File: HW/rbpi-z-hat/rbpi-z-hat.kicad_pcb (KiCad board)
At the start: 4 copper layers, 65 x 30 mm, 96 parts, among them IC1 BQ24315DSGR, J1 RBPI_CONN, J10 JST_GH, J2 Conn_01x10, J3 Conn_01x10, J4 Conn_01x10, J5 Conn_01x06, J6 Conn_01x06, J7 Conn_01x06, J8 Conn_01x06_MountingPin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

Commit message: Some changes in Sch & PCB
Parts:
- L5, L6, L7, L8: moved to B.Cu
- moved C1 81.6 mm to (24.8, 46.8)
- moved L8 46.3 mm to (36.8, 7.75)
- moved L7 46.2 mm to (35.0, 7.75)
- moved C23 42.8 mm to (25.0, 18.0), turned to 180 degrees
- moved L6 42.5 mm to (33.2, 7.75)
- moved L5 42.4 mm to (31.5, 7.75)
- moved C25 41.5 mm to (25.1, 16.0), turned to 180 degrees
- moved C26 40.6 mm to (25.1, 14.4), turned to 180 degrees
- moved C30 40.1 mm to (32.8, 15.0), turned to 270 degrees
- moved C27 39.9 mm to (28.1, 19.3), turned to 270 degrees
- moved C24 37.9 mm to (29.7, 19.3), turned to 270 degrees
- moved U8 35.5 mm to (29.2, 15.0), turned to 90 degrees
- moved U9 35.2 mm to (35.8, 15.0), turned to 180 degrees
- moved C28 35.2 mm to (34.8, 11.4), turned to 90 degrees
- moved C29 32.6 mm to (36.8, 11.6), turned to 90 degrees
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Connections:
- J1 pad 19: /rbpi/SPI0_MOSI -> /SPI0_MOSI
- J1 pad 21: /rbpi/SPI0_MISO -> /SPI0_MISO
- J1 pad 23: /rbpi/SPI0_SCLK -> /SPI0_SCK
- L5 pad 1: (no net) -> /SENS_MOSI
- L5 pad 2: (no net) -> /SPI0_MOSI
- L6 pad 1: (no net) -> /SENS_MISO
- L6 pad 2: (no net) -> /SPI0_MISO
- L7 pad 1: (no net) -> /SENS_SCK
- L7 pad 2: (no net) -> /SPI0_SCK
- RN7 pad 1: /rbpi/SPI0_MOSI -> /SPI0_MOSI
- RN7 pad 2: /rbpi/SPI0_MISO -> /SPI0_MISO
- RN7 pad 3: /rbpi/SPI0_SCLK -> /SPI0_SCK
- U6 pad 10: (no net) -> /SCL1
- U6 pad 9: (no net) -> /SDA1
- U8 pad 2: /IMU/IMU_SCK -> /SENS_SCK
- U8 pad 4: /IMU/IMU_MOSI -> /SENS_MOSI
- U8 pad 5: /IMU/IMU_MISO -> /SENS_MISO
- U8 pad 6: /IMU/IMU_MISO -> /SENS_MISO
- U9 pad 1: /IMU/IMU_MISO -> /SENS_MISO
- U9 pad 13: /IMU/IMU_SCK -> /SENS_SCK
- U9 pad 14: /IMU/IMU_MOSI -> /SENS_MOSI

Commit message: Changes in Sch
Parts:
- removed C20, C21: 22uF/10V, Capacitor_SMD:C_1206_3216Metric
- removed U7: MIC5504-3.3YM5, Package_TO_SOT_SMD:SOT-23-5
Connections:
- net /SENSORS_POWER/sheet5EE7A825/MIC_VIN renamed /SENSORS_POWER/MIC5504/MIC_VIN
- C12 pad 1: /SENSORS_POWER/SENS_VIN -> /BQ24313_OUT
- C12 pad 2: /SENSORS_POWER/SENS_GND -> GNDD
- IC1 pad 8: /BQ24313/BQ_OUT -> /BQ24313_OUT
- L2 pad 1: /SENSORS_POWER/SENS_VIN -> /BQ24313_OUT
- L3 pad 1: /SENSORS_POWER/SENS_GND -> GNDD

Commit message: Changes in Schematics
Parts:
- added R11: 10K, Resistor_SMD:R_0603_1608Metric, F.Cu at (21.6, -12.3)
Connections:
- net /PCA9685/PCA_nOE renamed /PCA_nOE
- net /rbpi/SPI1_CE2 renamed /rbpi/SPI0_CE0
- J1 pad 26: (no net) -> /rbpi/SPI0_CE1
- J1 pad 7: /rbpi/Pin_7_PPM_SBUS_INPUT -> /rbpi/GPIO_4
- R6 pad 1: (no net) -> /rbpi/GPIO_4
- RN6 pad 3: /rbpi/Pin_7_PPM_SBUS_INPUT -> /rbpi/GPIO_4
- U2 pad 6: /BARO/BARO_MISO -> /SENS_MISO
- U2 pad 7: /BARO/BARO_MOSI -> /SENS_MOSI
- U2 pad 8: /BARO/BARO_SCK -> /SENS_SCK
- U5 pad 3: /BARO/BARO_MOSI -> /SENS_MOSI
- U5 pad 4: /BARO/BARO_SCK -> /SENS_SCK
- U5 pad 5: /BARO/BARO_MISO -> /SENS_MISO

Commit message: Update
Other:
- net class 6mils removed
- net class Default removed

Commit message: Some new things...
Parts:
- added U7: STM32F031G6Ux, Package_DFN_QFN:QFN-28-1EP_4x4mm_P0.4mm_EP2.6x2.6mm_ThermalVias, F.Cu at (41.3, 16.6)
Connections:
- net /rbpi/GPIO_4 renamed /rbpi/Pin_7_PPM_SBUS_INPUT
- net Net-(J3-Pad1) renamed /PCA9685/SERVO_POWER
- IC1 pad 3: (no net) -> unconnected-(IC1-NC-Pad3)
- IC1 pad 4: (no net) -> /BQ24313/BQ_nFAULT
- J1 pad 11: (no net) -> /rbpi/Pin_11_UART_RTS
- J1 pad 12: (no net) -> /rbpi/Pin_12_UART_CTS
- J1 pad 13: (no net) -> /rbpi/Pin_13_PWM_EN
- J1 pad 15: (no net) -> /rbpi/GPIO_22
- J1 pad 16: (no net) -> /rbpi/Pin_16_MPU_DRDY
- J1 pad 18: (no net) -> /rbpi/Pin_18
- J1 pad 22: (no net) -> /rbpi/Pin_22
- J1 pad 24: /rbpi/SPI0_CE0 -> /LSM_nCS
- J1 pad 26: /rbpi/SPI0_CE1 -> /BMP_nCS
- J1 pad 27: (no net) -> /rbpi/GPIO_0_HAT_SDA
- J1 pad 28: (no net) -> /rbpi/GPIO_1_HAT_SCL
- J1 pad 29: (no net) -> /rbpi/GPIO_5
- J1 pad 31: (no net) -> /rbpi/GPIO_6
- J1 pad 32: (no net) -> /rbpi/GPIO_12
- J1 pad 33: (no net) -> /rbpi/GPIO_13
- J1 pad 35: (no net) -> /rbpi/GPIO_19
- J1 pad 36: (no net) -> /rbpi/Pin_36
- J1 pad 37: (no net) -> /rbpi/GPIO_26
- J1 pad 38: (no net) -> /rbpi/Pin_38
- J1 pad 40: (no net) -> /rbpi/Pin_40
- L8 pad 1: (no net) -> /FB/Y4
- L8 pad 2: (no net) -> /FB/X4
- R11 pad 2: /rbpi/SPI0_CE1 -> /BMP_nCS
- RN6 pad 4: (no net) -> unconnected-(RN6-R4.1-Pad4)
- RN6 pad 6: (no net) -> /rbpi/SBUS_INPUT_RAW
- RN7 pad 4: /rbpi/SPI0_CE0 -> /LSM_nCS
- U1 pad 3: (no net) -> /SENSORS_EN
- U1 pad 4: (no net) -> unconnected-(U1-NC-Pad4)
- U5 pad 2: (no net) -> /BMP_nCS
- U6 pad 2: (no net) -> unconnected-(U6-ALERT/RDY-Pad2)
- U6 pad 6: (no net) -> /ADS1015/AIN2
- U6 pad 7: (no net) -> /ADS1015/AIN3
- U8 pad 10: (no net) -> /IMU/LSM_INT3
- U8 pad 11: (no net) -> /IMU/LSM_INT1
- U8 pad 12: (no net) -> /IMU/LSM_INT2
- U8 pad 13: (no net) -> /IMU/LSM_DEN
- U8 pad 7: /IMU/LSM_nCS -> /LSM_nCS
- U8 pad 8: /IMU/LSM_nCS -> /LSM_nCS
- U8 pad 9: (no net) -> /IMU/LSM_INT4
- U9 pad 10: Net-(U9-Pad10) -> unconnected-(U9-RESV-Pad10)
- U9 pad 11: Net-(U9-Pad10) -> unconnected-(U9-RESV-Pad11)
- U9 pad 12: (no net) -> /IMU/ICM_nCS
- U9 pad 2: Net-(U9-Pad10) -> unconnected-(U9-RESV-Pad2)
- U9 pad 3: Net-(U9-Pad10) -> unconnected-(U9-RESV-Pad3)
- U9 pad 4: (no net) -> /IMU/ICM_INT1
- U9 pad 7: Net-(U9-Pad10) -> unconnected-(U9-RESV-Pad7)
- U9 pad 9: (no net) -> /IMU/ICM_INT2
- X1 pad 1: (no net) -> unconnected-(X1-EN-Pad1)

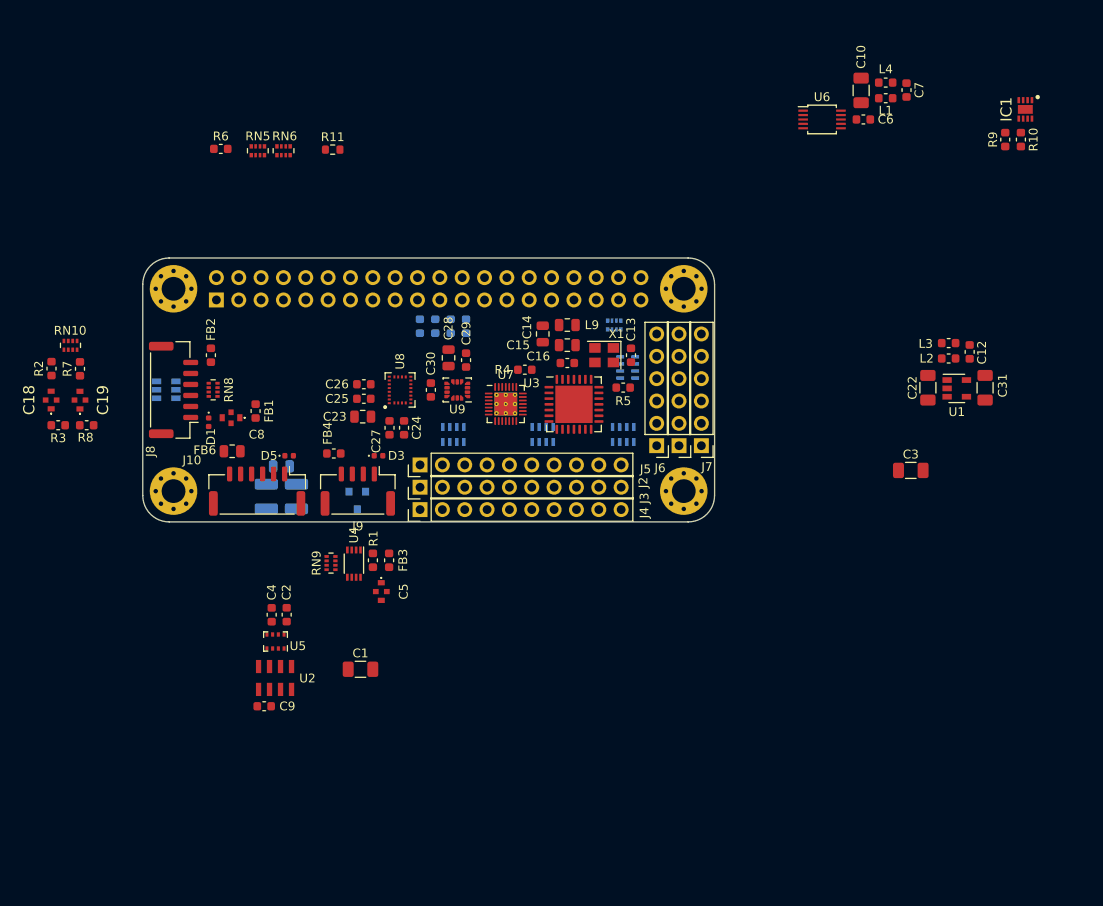
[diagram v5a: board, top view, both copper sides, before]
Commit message: PCA and ADC replaced by CH32V203G6U6
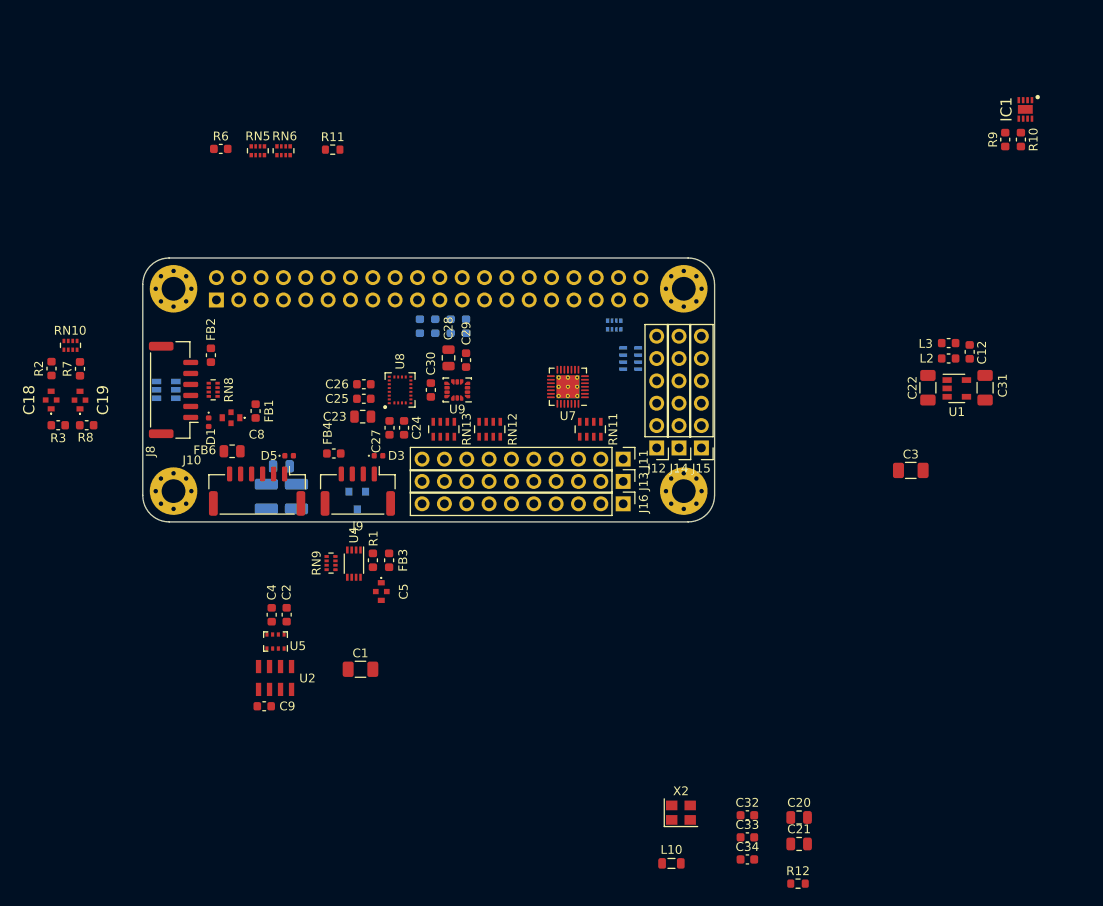
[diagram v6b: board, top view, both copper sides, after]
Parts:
- removed C10: 22uF/10V, Capacitor_SMD:C_1206_3216Metric
- removed C13, C16, C6: 0.1uF, Capacitor_SMD:C_0603_1608Metric
- removed C14, C15: 10uF, Capacitor_SMD:C_0805_2012Metric
- removed C7: 100nF, Capacitor_SMD:C_0603_1608Metric
- removed J2, J3, J4: Conn_01x10, Connector_PinHeader_2.54mm:PinHeader_1x10_P2.54mm_Vertical
- removed J5, J6, J7: Conn_01x06, Connector_PinHeader_2.54mm:PinHeader_1x06_P2.54mm_Vertical
- removed L1, L4: Ferrite_Bead, Inductor_SMD:L_0603_1608Metric
- removed L9: Ferrite_Bead, Inductor_SMD:L_0805_2012Metric
- removed R4, R5: 10K, Resistor_SMD:R_0603_1608Metric
- removed RN1, RN2, RN3, RN4: 220R, Resistor_SMD:R_Array_Concave_4x0603
- removed U3: PCA9685BS, Package_DFN_QFN:QFN-28-1EP_6x6mm_P0.65mm_EP4.25x4.25mm
- removed U6: ADS1015IDGS, Package_SO:TSSOP-10_3x3mm_P0.5mm
- removed X1: ASEMB-25.000MHZ-LC-T, Oscillator:Oscillator_SMD_Abracon_ASE-4Pin_3.2x2.5mm
- added C20: 10uF, Capacitor_SMD:C_0805_2012Metric, F.Cu at (74.6, 63.6)
- added C21: 10uF, Capacitor_SMD:C_0805_2012Metric, F.Cu at (74.6, 66.6)
- added C32: 0.1uF, Capacitor_SMD:C_0603_1608Metric, F.Cu at (68.7, 63.4)
- added C33: 0.1uF, Capacitor_SMD:C_0603_1608Metric, F.Cu at (68.7, 65.9)
- added C34: 0.1uF, Capacitor_SMD:C_0603_1608Metric, F.Cu at (68.7, 68.4)
- added J11: Conn_01x10, Connector_PinHeader_2.54mm:PinHeader_1x10_P2.54mm_Vertical, F.Cu at (54.6, 22.9)
- added J12: Conn_01x06, Connector_PinHeader_2.54mm:PinHeader_1x06_P2.54mm_Vertical, F.Cu at (58.4, 21.6)
- added J13: Conn_01x10, Connector_PinHeader_2.54mm:PinHeader_1x10_P2.54mm_Vertical, F.Cu at (54.6, 25.4)
- added J14: Conn_01x06, Connector_PinHeader_2.54mm:PinHeader_1x06_P2.54mm_Vertical, F.Cu at (61.0, 21.6)
- added J15: Conn_01x06, Connector_PinHeader_2.54mm:PinHeader_1x06_P2.54mm_Vertical, F.Cu at (63.5, 21.6)
- added J16: Conn_01x10, Connector_PinHeader_2.54mm:PinHeader_1x10_P2.54mm_Vertical, F.Cu at (54.6, 27.9)
- added L10: Ferrite_Bead, Inductor_SMD:L_0805_2012Metric, F.Cu at (60.1, 68.8)
- added R12: 10K, Resistor_SMD:R_0603_1608Metric, F.Cu at (74.5, 71.1)
- added RN11: 220R, Resistor_SMD:R_Array_Concave_4x0603, F.Cu at (50.9, 19.5)
- added RN12: 220R, Resistor_SMD:R_Array_Concave_4x0603, F.Cu at (39.4, 19.5)
- added RN13: 220R, Resistor_SMD:R_Array_Concave_4x0603, F.Cu at (34.2, 19.5)
- added RN14: 220R, Resistor_SMD:R_Array_Concave_4x0603, B.Cu at (55.5, 11.4)
- added X2: ASEMB-25.000MHZ-LC-T, Oscillator:Oscillator_SMD_Abracon_ASE-4Pin_3.2x2.5mm, F.Cu at (61.2, 63.1)
- moved U7 7.33 mm to (48.3, 14.6), turned to 180 degrees
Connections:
- U7 pad 10: unconnected-(U7-PA4-Pad10) -> /SDA1
- U7 pad 11: unconnected-(U7-PA5-Pad11) -> /CH32V203G6U6/PWM_OUT7
- U7 pad 12: unconnected-(U7-PA6-Pad12) -> /CH32V203G6U6/PWM_OUT8
- U7 pad 13: unconnected-(U7-PA7-Pad13) -> /CH32V203G6U6/PWM_OUT9
- U7 pad 14: unconnected-(U7-PB0-Pad14) -> /CH32V203G6U6/PWM_OUT0
- U7 pad 15: unconnected-(U7-PB1-Pad15) -> /CH32V203G6U6/PWM_OUT1
- U7 pad 16: unconnected-(U7-VSS-Pad16) -> GNDD
- U7 pad 17: unconnected-(U7-VDD-Pad17) -> /CH32V203G6U6/CH32_VDD
- U7 pad 18: unconnected-(U7-PA8-Pad18) -> /CH32V203G6U6/PWM_OUT10
- U7 pad 19: unconnected-(U7-PA9-Pad19) -> /CH32V203G6U6/PWM_OUT11
- U7 pad 2: unconnected-(U7-PF0-Pad2) -> /CH32V203G6U6/CH32_EXTCLK
- U7 pad 20: unconnected-(U7-PA10-Pad20) -> /CH32V203G6U6/PWM_OUT12
- U7 pad 21: unconnected-(U7-PA13-Pad21) -> /CH32V203G6U6/PWM_OUT13
- U7 pad 22: unconnected-(U7-PA14-Pad22) -> /CH32V203G6U6/PWM_OUT14
- U7 pad 23: unconnected-(U7-PA15-Pad23) -> /CH32V203G6U6/PWM_OUT15
- U7 pad 24: unconnected-(U7-PB3-Pad24) -> /CH32V203G6U6/PWM_OUT2
- U7 pad 25: unconnected-(U7-PB4-Pad25) -> /CH32V203G6U6/PWM_OUT3
- U7 pad 26: unconnected-(U7-PB5-Pad26) -> /CH32V203G6U6/PWM_OUT4
- U7 pad 27: unconnected-(U7-PB6-Pad27) -> /CH32V203G6U6/PWM_OUT5
- U7 pad 28: unconnected-(U7-PB7-Pad28) -> /CH32V203G6U6/PWM_OUT6
- U7 pad 3: unconnected-(U7-PF1-Pad3) -> /PCA_nOE
- U7 pad 5: unconnected-(U7-VDDA-Pad5) -> /CH32V203G6U6/CH32_VDD
- U7 pad 6: unconnected-(U7-PA0-Pad6) -> /CUR_SENS
- U7 pad 7: unconnected-(U7-PA1-Pad7) -> /VOLT_SENS
- U7 pad 8: unconnected-(U7-PA2-Pad8) -> /CH32V203G6U6/ADC3
- U7 pad 9: unconnected-(U7-PA3-Pad9) -> /SCL1

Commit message: Some update...
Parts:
- moved C32 11.6 mm to (57.1, 63.4), turned to -90 degrees
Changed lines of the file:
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@@
   (paper "A4" portrait)
   (title_block
-    (title "Raspberri Pi Zero Hat")
+    (title "RasPi Zero NAV Hat")
     (date "2020-06-02")
     (rev "0.1")
     (company "chipiki.ru")
+    (comment 1 "RasPi Zero NAV Hat")
   )
   (layers
@@
   )
   (setup
+    (stackup
+      (layer "F.SilkS" (type "Top Silk Screen"))
+      (layer "F.Paste" (type "Top Solder Paste"))
+      (layer "F.Mask" (type "Top Solder Mask") (thickness 0.01))
+      (layer "F.Cu" (type "copper") (thickness 0.035))
+      (layer "dielectric 1" (type "core") (thickness 0.48) (material "FR4") (epsilon_r 4.5) (loss_tangent 0.02))
+      (layer "In1.Cu" (type "copper") (thickness 0.035))
+      (layer "dielectric 2" (type "prepreg") (thickness 0.48) (material "FR4") (epsilon_r 4.5) (loss_tangent 0.02))
+      (layer "In2.Cu" (type "copper") (thickness 0.035))
+      (layer "dielectric 3" (type "core") (thickness 0.48) (material "FR4") (epsilon_r 4.5) (loss_tangent 0.02))
+      (layer "B.Cu" (type "copper") (thickness 0.035))
+      (layer "B.Mask" (type "Bottom Solder Mask") (thickness 0.01))
+      (layer "B.Paste" (type "Bottom Solder Paste"))
+      (layer "B.SilkS" (type "Bottom Silk Screen"))
+      (copper_finish "None")
+      (dielectric_constraints no)
+    )
     (pad_to_mask_clearance 0.05)
     (pcbplotparams
@@
   )
   (footprint "Capacitor_SMD:C_0603_1608Metric" (layer "F.Cu")
-    (at 68.73 63.35)
+    (at 57.15 63.35 -90)
     (descr "Capacitor SMD 0603 (1608 Metric), square (rectangular) end terminal, IPC_7351 nominal, (Body size source: IPC-SM-782 page 76, https://www.pcb-3d.com/wordpress/wp-content/uploads/ipc-sm-782a_amendment_1_and_2.pdf), generated with kicad-footprint-generator")
     (tags "capacitor")
@@
     (property "ki_keywords" "cap capacitor")
     (attr smd)
-    (fp_text reference "C32" (at 0 -1.43) (layer "F.SilkS")
+    (fp_text reference "C32" (at 0 -1.43 90) (layer "F.SilkS")
         (effects (font (size 1 1) (thickness 0.15)))
     )
-    (fp_text value "0.1uF" (at 0 1.43) (layer "F.Fab")
+    (fp_text value "0.1uF" (at 0 1.43 90) (layer "F.Fab")
         (effects (font (size 1 1) (thickness 0.15)))
     )
-    (fp_text user "${REFERENCE}" (at 0 0) (layer "F.Fab")
+    (fp_text user "${REFERENCE}" (at 0 0 90) (layer "F.Fab")
         (effects (font (size 0.4 0.4) (thickness 0.06)))
     )
@@
     (fp_line (start 0.8 0.4) (end -0.8 0.4)
       (stroke (width 0.1) (type solid)) (layer "F.Fab"))
-    (pad "1" smd roundrect (at -0.775 0) (size 0.9 0.95) (layers "F.Cu" "F.Paste" "F.Mask") (roundrect_rratio 0.25)
+    (pad "1" smd roundrect (at -0.775 0 270) (size 0.9 0.95) (layers "F.Cu" "F.Paste" "F.Mask") (roundrect_rratio 0.25)
       (net 81 "/CH32V203G6U6/CH32_VDD") (pintype "passive"))
-    (pad "2" smd roundrect (at 0.775 0) (size 0.9 0.95) (layers "F.Cu" "F.Paste" "F.Mask") (roundrect_rratio 0.25)
+    (pad "2" smd roundrect (at 0.775 0 270) (size 0.9 0.95) (layers "F.Cu" "F.Paste" "F.Mask") (roundrect_rratio 0.25)
       (net 1 "GNDD") (pintype "passive"))
     (model "${KICAD6_3DMODEL_DIR}/Capacitor_SMD.3dshapes/C_0603_1608Metric.wrl"

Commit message: Apdated Sch and PCB
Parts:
- added C10: 4.7uF, Capacitor_SMD:C_0402_1005Metric, F.Cu at (83.5, 45.5)
- added C13: 0.1uF, Capacitor_SMD:C_0402_1005Metric, F.Cu at (90.0, 41.5)
- added C14: 4.7uF, Capacitor_SMD:C_0402_1005Metric, F.Cu at (90.0, 43.5)
- added C15: 0.1uF, Capacitor_SMD:C_0402_1005Metric, F.Cu at (90.0, 45.5)
- added C6: 0.1uF, Capacitor_SMD:C_0402_1005Metric, F.Cu at (83.5, 41.5)
- added C7: 0.1uF, Capacitor_SMD:C_0402_1005Metric, F.Cu at (83.5, 43.5)
- added JP1: SolderJumper_3_Open, Jumper:SolderJumper-3_P1.3mm_Open_RoundedPad1.0x1.5mm_NumberLabels, F.Cu at (79.2, 42.3)
- added JP3: SolderJumper_3_Open, Jumper:SolderJumper-3_P1.3mm_Open_RoundedPad1.0x1.5mm_NumberLabels, F.Cu at (79.2, 45.9)
- added U3: IST8310, Package_LGA:LGA-16_3x3mm_P0.5mm, F.Cu at (84.3, 48.7)
- added U6: MMC5883MA, Package_LGA:LGA-16_3x3mm_P0.5mm, F.Cu at (93.7, 42.8)
